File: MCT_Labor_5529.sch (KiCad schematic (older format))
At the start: 4 parts

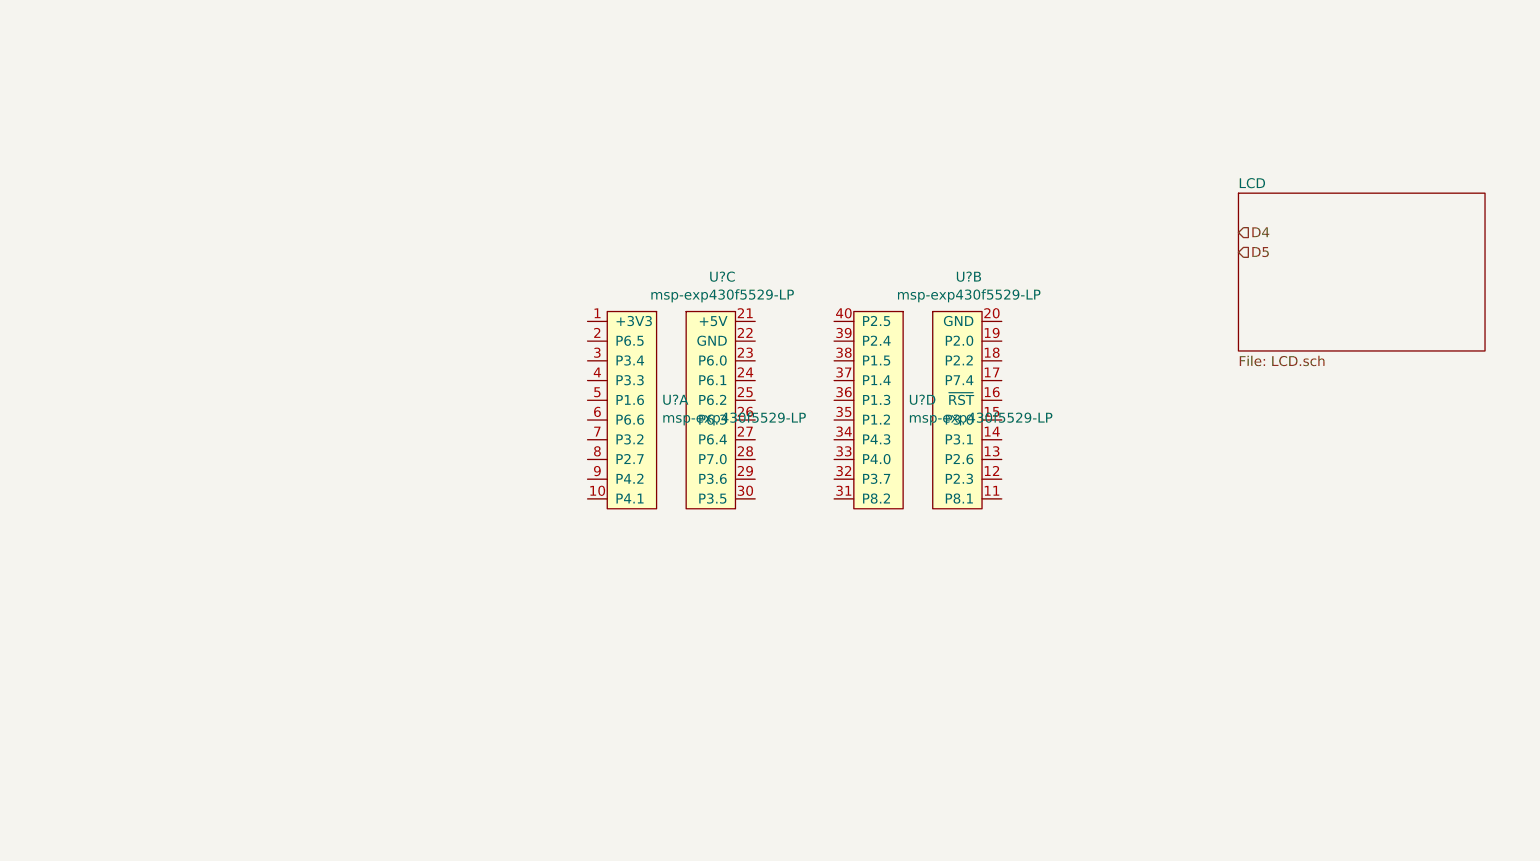
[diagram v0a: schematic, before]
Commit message: Schaltplan angefangen
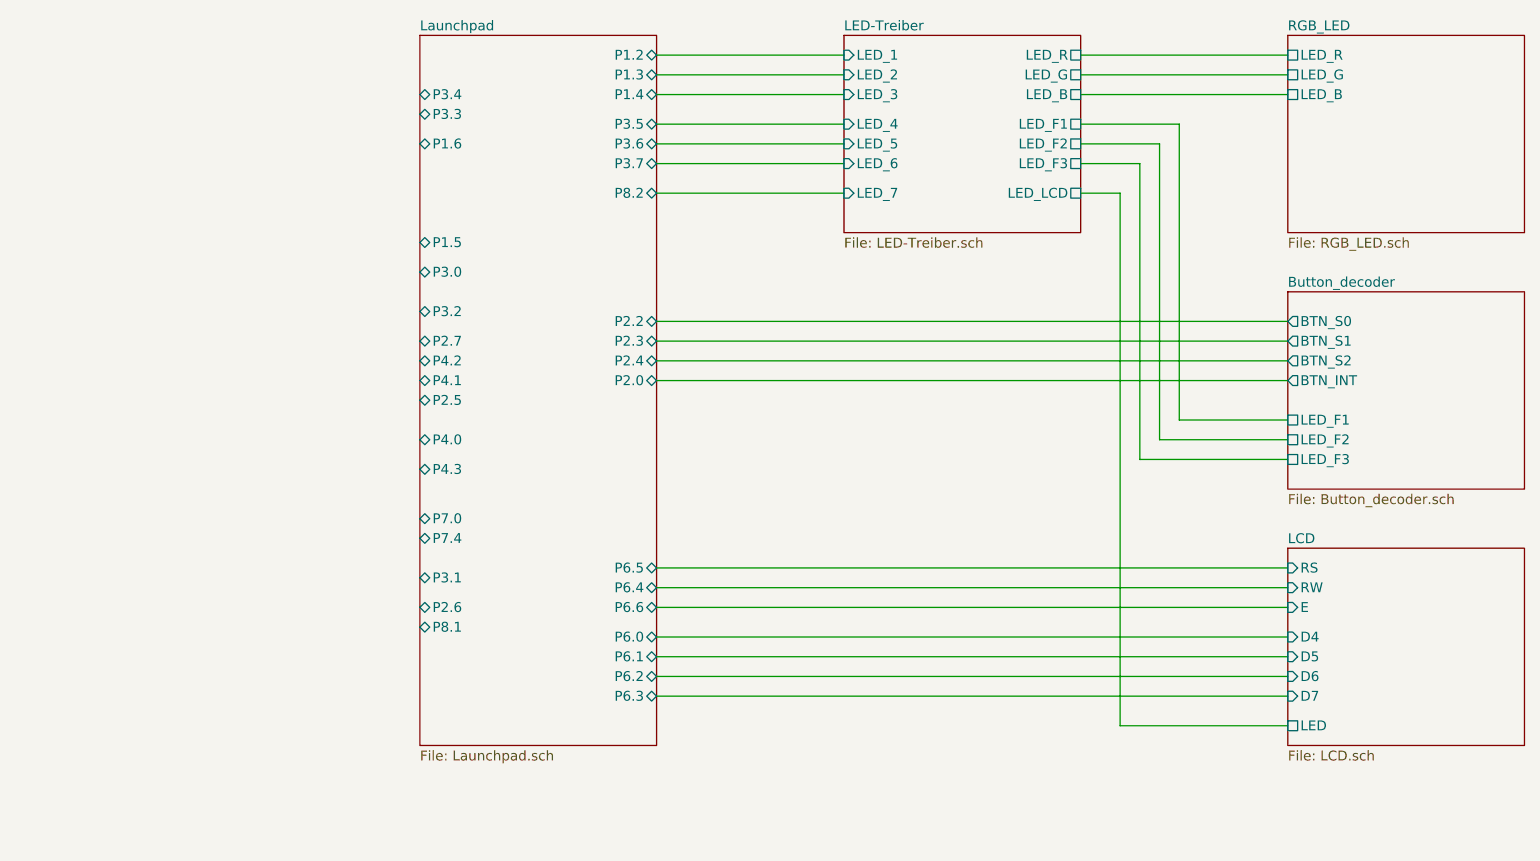
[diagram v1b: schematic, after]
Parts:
- removed U? (x4): msp-exp430f5529-LP, symbol HS-Wismar:msp-exp430f5529-LP
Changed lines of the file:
@@
 $Descr A4 11693 8268
 encoding utf-8
-Sheet 1 2
+Sheet 1 6
 Title ""
 Date ""
@@
 Comment4 ""
 $EndDescr
-$Comp
-L HS-Wismar:msp-exp430f5529-LP U?
-U 1 1 5EE8B2E3
-P 5550 3950
-F 0 "U?" H 5522 4501 50  0000 R CNN
-F 1 "msp-exp430f5529-LP" H 5522 4410 50  0000 R CNN
-F 2 "" H 5550 3950 50  0001 C CNN
-F 3 "" H 5550 3950 50  0001 C CNN
-	1    5550 3950
-	-1   0    0    -1
-$EndComp
-$Comp
-L HS-Wismar:msp-exp430f5529-LP U?
-U 2 1 5EE8BD9B
-P 6950 3950
-F 0 "U?" H 7133 5125 50  0000 C CNN
-F 1 "msp-exp430f5529-LP" H 7133 5034 50  0000 C CNN
-F 2 "" H 6950 3950 50  0001 C CNN
-F 3 "" H 6950 3950 50  0001 C CNN
-	2    6950 3950
-	1    0    0    -1
-$EndComp
-$Comp
-L HS-Wismar:msp-exp430f5529-LP U?
-U 3 1 5EE8C0BE
-P 5700 3950
-F 0 "U?" H 5883 5125 50  0000 C CNN
-F 1 "msp-exp430f5529-LP" H 5883 5034 50  0000 C CNN
-F 2 "" H 5700 3950 50  0001 C CNN
-F 3 "" H 5700 3950 50  0001 C CNN
-	3    5700 3950
-	1    0    0    -1
-$EndComp
-$Comp
-L HS-Wismar:msp-exp430f5529-LP U?
-U 4 1 5EE8CABB
-P 6800 3950
-F 0 "U?" H 6772 4501 50  0000 R CNN
-F 1 "msp-exp430f5529-LP" H 6772 4410 50  0000 R CNN
-F 2 "" H 6800 3950 50  0001 C CNN
-F 3 "" H 6800 3950 50  0001 C CNN
-	4    6800 3950
-	-1   0    0    -1
-$EndComp
 $Sheet
-S 8500 2350 1250 800
+S 8750 4150 1200 1000
 U 5EE928F9
 F0 "LCD" 50
 F1 "LCD.sch" 50
+F2 "D4" I L 8750 4600 50
+F3 "D5" I L 8750 4700 50
+F4 "D6" I L 8750 4800 50
+F5 "D7" I L 8750 4900 50
+F6 "RS" I L 8750 4250 50
+F7 "RW" I L 8750 4350 50
+F8 "E" I L 8750 4450 50
+F9 "LED" U L 8750 5050 50
 $EndSheet
-Text HLabel 8500 2550 2    50   Input ~ 0
-D4
-Text HLabel 8500 2650 2    50   Input ~ 0
-D5
+Wire Wire Line
+	8750 4900 5550 4900
+$Sheet
+S 6500 1550 1200 1000
+U 5EF68F99
+F0 "LED-Treiber" 50
+F1 "LED-Treiber.sch" 50
+F2 "LED_1" I L 6500 1650 50
+F3 "LED_2" I L 6500 1750 50
+F4 "LED_3" I L 6500 1850 50
+F5 "LED_4" I L 6500 2000 50
+F6 "LED_5" I L 6500 2100 50
+F7 "LED_6" I L 6500 2200 50
+F8 "LED_7" I L 6500 2350 50
+F9 "LED_R" U R 7700 1650 50
+F10 "LED_G" U R 7700 1750 50
+F11 "LED_B" U R 7700 1850 50
+F12 "LED_F1" U R 7700 2000 50
+F13 "LED_F2" U R 7700 2100 50
+F14 "LED_F3" U R 7700 2200 50
+F15 "LED_LCD" U R 7700 2350 50
+$EndSheet
+Wire Wire Line
+	7700 2350 7900 2350
+Wire Wire Line
+	7900 2350 7900 5050
+Wire Wire Line
+	7900 5050 8750 5050
+Wire Wire Line
+	6500 1650 5550 1650
+Wire Wire Line
+	5550 1750 6500 1750
+Wire Wire Line
+	6500 1850 5550 1850
+Wire Wire Line
+	5550 2000 6500 2000
+Wire Wire Line
+	5550 2100 6500 2100
+Wire Wire Line
+	5550 2200 6500 2200
+Wire Wire Line
+	5550 2350 6500 2350
+$Sheet
+S 8750 2850 1200 1000
+U 5EFA716B
+F0 "Button_decoder" 50
+F1 "Button_decoder.sch" 50
+F2 "BTN_S0" O L 8750 3000 50
+F3 "BTN_S1" O L 8750 3100 50
+F4 "BTN_S2" O L 8750 3200 50
+F5 "BTN_INT" O L 8750 3300 50
+F6 "LED_F1" U L 8750 3500 50
+F7 "LED_F2" U L 8750 3600 50
+F8 "LED_F3" U L 8750 3700 50
+$EndSheet
+Wire Wire Line
+	8200 2000 8200 3500
+Wire Wire Line
+	8200 3500 8750 3500
+Wire Wire Line
+	7700 2000 8200 2000
+Wire Wire Line
+	8750 3600 8100 3600
+Wire Wire Line
+	8100 3600 8100 2100
+Wire Wire Line
+	8100 2100 7700 2100
+Wire Wire Line
+	7700 2200 8000 2200
+Wire Wire Line
+	8000 2200 8000 3700
+Wire Wire Line
+	8000 3700 8750 3700
+$Sheet
+S 8750 1550 1200 1000
+U 5F03A5E7
+F0 "RGB_LED" 50
+F1 "RGB_LED.sch" 50
+F2 "LED_R" U L 8750 1650 50
+F3 "LED_G" U L 8750 1750 50
+F4 "LED_B" U L 8750 1850 50
+$EndSheet
+Wire Wire Line
+	7700 1650 8750 1650
+Wire Wire Line
+	8750 1750 7700 1750
+Wire Wire Line
+	7700 1850 8750 1850
+Wire Wire Line
+	5550 4800 8750 4800
+Wire Wire Line
+	5550 4700 8750 4700
+Wire Wire Line
+	5550 4600 8750 4600
+Wire Wire Line
+	5550 4450 8750 4450
+Wire Wire Line
+	5550 4350 8750 4350
+Wire Wire Line
+	5550 4250 8750 4250
+Wire Wire Line
+	5550 3300 8750 3300
+Wire Wire Line
+	5550 3200 8750 3200
+Wire Wire Line
+	5550 3100 8750 3100
+Wire Wire Line
+	5550 3000 8750 3000
+$Sheet
+S 4350 1550 1200 3600
+U 5F0B42CA
+F0 "Launchpad" 50
+F1 "Launchpad.sch" 50
+F2 "P6.5" B R 5550 4250 50
+F3 "P3.4" B L 4350 1850 50
+F4 "P3.3" B L 4350 1950 50
+F5 "P1.6" B L 4350 2100 50
+F6 "P6.6" B R 5550 4450 50
+F7 "P3.2" B L 4350 2950 50
+F8 "P2.7" B L 4350 3100 50
+F9 "P4.2" B L 4350 3200 50
+F10 "P4.1" B L 4350 3300 50
+F11 "P2.5" B L 4350 3400 50
+F12 "P2.4" B R 5550 3200 50
+F13 "P1.5" B L 4350 2600 50
+F14 "P1.4" B R 5550 1850 50
+F15 "P1.3" B R 5550 1750 50
+F16 "P1.2" B R 5550 1650 50
+F17 "P4.3" B L 4350 3750 50
+F18 "P4.0" B L 4350 3600 50
+F19 "P3.7" B R 5550 2200 50
+F20 "P8.2" B R 5550 2350 50
+F21 "P6.0" B R 5550 4600 50
+F22 "P6.1" B R 5550 4700 50
+F23 "P6.2" B R 5550 4800 50
+F24 "P6.3" B R 5550 4900 50
+F25 "P6.4" B R 5550 4350 50
+F26 "P7.0" B L 4350 4000 50
+F27 "P3.6" B R 5550 2100 50
+F28 "P3.5" B R 5550 2000 50
+F29 "P2.0" B R 5550 3300 50
+F30 "P2.2" B R 5550 3000 50
+F31 "P7.4" B L 4350 4100 50
+F32 "P3.0" B L 4350 2750 50
+F33 "P3.1" B L 4350 4300 50
+F34 "P2.6" B L 4350 4450 50
+F35 "P2.3" B R 5550 3100 50
+F36 "P8.1" B L 4350 4550 50
+$EndSheet
 $EndSCHEMATC

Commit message: Blockschaltbild komplett v1
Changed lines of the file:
@@
 $Descr A4 11693 8268
 encoding utf-8
-Sheet 1 6
+Sheet 1 10
 Title ""
 Date ""
@@
 F1 "Launchpad.sch" 50
 F2 "P6.5" B R 5550 4250 50
-F3 "P3.4" B L 4350 1850 50
-F4 "P3.3" B L 4350 1950 50
-F5 "P1.6" B L 4350 2100 50
+F3 "P3.4" B L 4350 3250 50
+F4 "P3.3" B L 4350 3150 50
+F5 "P1.6" B L 4350 4850 50
 F6 "P6.6" B R 5550 4450 50
-F7 "P3.2" B L 4350 2950 50
-F8 "P2.7" B L 4350 3100 50
-F9 "P4.2" B L 4350 3200 50
-F10 "P4.1" B L 4350 3300 50
-F11 "P2.5" B L 4350 3400 50
+F7 "P3.2" B L 4350 1850 50
+F8 "P2.7" B L 4350 2650 50
+F9 "P4.2" B L 4350 4050 50
+F10 "P4.1" B L 4350 3950 50
+F11 "P2.5" B L 4350 2450 50
 F12 "P2.4" B R 5550 3200 50
-F13 "P1.5" B L 4350 2600 50
+F13 "P1.5" B L 4350 4750 50
 F14 "P1.4" B R 5550 1850 50
 F15 "P1.3" B R 5550 1750 50
 F16 "P1.2" B R 5550 1650 50
-F17 "P4.3" B L 4350 3750 50
-F18 "P4.0" B L 4350 3600 50
+F17 "P4.3" B L 4350 2200 50
+F18 "P4.0" B L 4350 2100 50
 F19 "P3.7" B R 5550 2200 50
 F20 "P8.2" B R 5550 2350 50
@@
 F24 "P6.3" B R 5550 4900 50
 F25 "P6.4" B R 5550 4350 50
-F26 "P7.0" B L 4350 4000 50
+F26 "P7.0" B L 4350 5050 50
 F27 "P3.6" B R 5550 2100 50
 F28 "P3.5" B R 5550 2000 50
 F29 "P2.0" B R 5550 3300 50
 F30 "P2.2" B R 5550 3000 50
-F31 "P7.4" B L 4350 4100 50
-F32 "P3.0" B L 4350 2750 50
-F33 "P3.1" B L 4350 4300 50
-F34 "P2.6" B L 4350 4450 50
+F31 "P7.4" B L 4350 2000 50
+F32 "P3.0" B L 4350 1650 50
+F33 "P3.1" B L 4350 1750 50
+F34 "P2.6" B L 4350 2550 50
 F35 "P2.3" B R 5550 3100 50
-F36 "P8.1" B L 4350 4550 50
-$EndSheet
+F36 "P8.1" B L 4350 2350 50
+F37 "~RST" O L 4350 3400 50
+$EndSheet
+$Sheet
+S 2300 1550 1200 1200
+U 5EF44B02
+F0 "SPI" 50
+F1 "SPI.sch" 50
+F2 "A0" I R 3500 2450 50
+F3 "A1" I R 3500 2550 50
+F4 "A2" I R 3500 2650 50
+F5 "ADDR_EN" I R 3500 2350 50
+F6 "MISO" O R 3500 1750 50
+F7 "MOSI" I R 3500 1650 50
+F8 "SCK" I R 3500 1850 50
+F9 "µSD_detect" O R 3500 2000 50
+F10 "NRF_CE" I R 3500 2100 50
+F11 "NRF_INT" O R 3500 2200 50
+$EndSheet
+Wire Wire Line
+	3500 1650 4350 1650
+Wire Wire Line
+	4350 1750 3500 1750
+Wire Wire Line
+	3500 1850 4350 1850
+Wire Wire Line
+	4350 2350 3500 2350
+Wire Wire Line
+	3500 2450 4350 2450
+Wire Wire Line
+	4350 2550 3500 2550
+Wire Wire Line
+	3500 2650 4350 2650
+$Sheet
+S 2300 3050 1200 500
+U 5EFA875F
+F0 "UART" 50
+F1 "UART.sch" 50
+F2 "RX_in" I R 3500 3150 50
+F3 "TX_out" O R 3500 3250 50
+F4 "~RST" I R 3500 3400 50
+$EndSheet
+$Sheet
+S 2300 3850 1200 500
+U 5EFA8860
+F0 "I2C" 50
+F1 "I2C.sch" 50
+F2 "SDA" B R 3500 3950 50
+F3 "SCL" I R 3500 4050 50
+$EndSheet
+Wire Wire Line
+	4350 2200 3500 2200
+Wire Wire Line
+	3500 2100 4350 2100
+Wire Wire Line
+	4350 2000 3500 2000
+$Sheet
+S 2300 4650 1200 500
+U 5EFB1255
+F0 "analog/Fan" 50
+F1 "analog.sch" 50
+F2 "pulse_out" O R 3500 4750 50
+F3 "PWM_in" I R 3500 4850 50
+F4 "analog" U R 3500 5050 50
+$EndSheet
+Wire Wire Line
+	4350 3400 3500 3400
+Wire Wire Line
+	4350 3150 3500 3150
+Wire Wire Line
+	3500 3250 4350 3250
+Wire Wire Line
+	3500 3950 4350 3950
+Wire Wire Line
+	3500 4050 4350 4050
+Wire Wire Line
+	3500 5050 4350 5050
+Wire Wire Line
+	4350 4850 3500 4850
+Wire Wire Line
+	3500 4750 4350 4750
 $EndSCHEMATC

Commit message: Erste fertige Version
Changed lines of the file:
@@
 $EndDescr
 $Sheet
-S 8750 4150 1200 1000
+S 8750 4550 1200 1000
 U 5EE928F9
 F0 "LCD" 50
 F1 "LCD.sch" 50
-F2 "D4" I L 8750 4600 50
-F3 "D5" I L 8750 4700 50
-F4 "D6" I L 8750 4800 50
-F5 "D7" I L 8750 4900 50
-F6 "RS" I L 8750 4250 50
-F7 "RW" I L 8750 4350 50
-F8 "E" I L 8750 4450 50
-F9 "LED" U L 8750 5050 50
-$EndSheet
-Wire Wire Line
-	8750 4900 5550 4900
+F2 "D4" I L 8750 5000 50
+F3 "D5" I L 8750 5100 50
+F4 "D6" I L 8750 5200 50
+F5 "D7" I L 8750 5300 50
+F6 "RS" I L 8750 4750 50
+F7 "R~W~" I L 8750 4650 50
+F8 "E" I L 8750 4850 50
+F9 "LED" U L 8750 5450 50
+$EndSheet
+Wire Wire Line
+	8750 5300 5550 5300
 $Sheet
 S 6500 1550 1200 1000
@@
 	7700 2350 7900 2350
 Wire Wire Line
-	7900 2350 7900 5050
-Wire Wire Line
-	7900 5050 8750 5050
+	7900 2350 7900 5450
+Wire Wire Line
+	7900 5450 8750 5450
 Wire Wire Line
 	6500 1650 5550 1650
@@
 	5550 2350 6500 2350
 $Sheet
-S 8750 2850 1200 1000
+S 8750 3000 1200 1000
 U 5EFA716B
 F0 "Button_decoder" 50
 F1 "Button_decoder.sch" 50
-F2 "BTN_S0" O L 8750 3000 50
-F3 "BTN_S1" O L 8750 3100 50
-F4 "BTN_S2" O L 8750 3200 50
-F5 "BTN_INT" O L 8750 3300 50
-F6 "LED_F1" U L 8750 3500 50
-F7 "LED_F2" U L 8750 3600 50
-F8 "LED_F3" U L 8750 3700 50
-$EndSheet
-Wire Wire Line
-	8200 2000 8200 3500
-Wire Wire Line
-	8200 3500 8750 3500
+F2 "BTN_S0" O L 8750 3150 50
+F3 "BTN_S1" O L 8750 3250 50
+F4 "BTN_S2" O L 8750 3350 50
+F5 "BTN_INT" O L 8750 3450 50
+F6 "LED_F1" U L 8750 3650 50
+F7 "LED_F2" U L 8750 3750 50
+F8 "LED_F3" U L 8750 3850 50
+$EndSheet
 Wire Wire Line
 	7700 2000 8200 2000
 Wire Wire Line
-	8750 3600 8100 3600
-Wire Wire Line
-	8100 3600 8100 2100
-Wire Wire Line
 	8100 2100 7700 2100
 Wire Wire Line
 	7700 2200 8000 2200
-Wire Wire Line
-	8000 2200 8000 3700
-Wire Wire Line
-	8000 3700 8750 3700
 $Sheet
 S 8750 1550 1200 1000
@@
 	7700 1850 8750 1850
 Wire Wire Line
-	5550 4800 8750 4800
-Wire Wire Line
-	5550 4700 8750 4700
-Wire Wire Line
-	5550 4600 8750 4600
-Wire Wire Line
-	5550 4450 8750 4450
-Wire Wire Line
-	5550 4350 8750 4350
-Wire Wire Line
-	5550 4250 8750 4250
-Wire Wire Line
-	5550 3300 8750 3300
-Wire Wire Line
-	5550 3200 8750 3200
-Wire Wire Line
-	5550 3100 8750 3100
-Wire Wire Line
-	5550 3000 8750 3000
-$Sheet
-S 4350 1550 1200 3600
-U 5F0B42CA
-F0 "Launchpad" 50
-F1 "Launchpad.sch" 50
-F2 "P6.5" B R 5550 4250 50
-F3 "P3.4" B L 4350 3250 50
-F4 "P3.3" B L 4350 3150 50
-F5 "P1.6" B L 4350 4850 50
-F6 "P6.6" B R 5550 4450 50
-F7 "P3.2" B L 4350 1850 50
-F8 "P2.7" B L 4350 2650 50
-F9 "P4.2" B L 4350 4050 50
-F10 "P4.1" B L 4350 3950 50
-F11 "P2.5" B L 4350 2450 50
-F12 "P2.4" B R 5550 3200 50
-F13 "P1.5" B L 4350 4750 50
-F14 "P1.4" B R 5550 1850 50
-F15 "P1.3" B R 5550 1750 50
-F16 "P1.2" B R 5550 1650 50
-F17 "P4.3" B L 4350 2200 50
-F18 "P4.0" B L 4350 2100 50
-F19 "P3.7" B R 5550 2200 50
-F20 "P8.2" B R 5550 2350 50
-F21 "P6.0" B R 5550 4600 50
-F22 "P6.1" B R 5550 4700 50
-F23 "P6.2" B R 5550 4800 50
-F24 "P6.3" B R 5550 4900 50
-F25 "P6.4" B R 5550 4350 50
-F26 "P7.0" B L 4350 5050 50
-F27 "P3.6" B R 5550 2100 50
-F28 "P3.5" B R 5550 2000 50
-F29 "P2.0" B R 5550 3300 50
-F30 "P2.2" B R 5550 3000 50
-F31 "P7.4" B L 4350 2000 50
-F32 "P3.0" B L 4350 1650 50
-F33 "P3.1" B L 4350 1750 50
-F34 "P2.6" B L 4350 2550 50
-F35 "P2.3" B R 5550 3100 50
-F36 "P8.1" B L 4350 2350 50
-F37 "~RST" O L 4350 3400 50
-$EndSheet
+	5550 5200 8750 5200
+Wire Wire Line
+	5550 5100 8750 5100
+Wire Wire Line
+	5550 5000 8750 5000
+Wire Wire Line
+	5550 4850 8750 4850
+Wire Wire Line
+	5550 4750 8750 4750
+Wire Wire Line
+	5550 4650 8750 4650
+Wire Wire Line
+	5550 3250 8750 3250
+Wire Wire Line
+	5550 3150 8750 3150
+Wire Wire Line
+	5550 3350 8750 3350
+Wire Wire Line
+	5550 3450 8750 3450
 $Sheet
 S 2300 1550 1200 1200
@@
 	3500 2650 4350 2650
 $Sheet
-S 2300 3050 1200 500
+S 2300 3050 1200 900
 U 5EFA875F
 F0 "UART" 50
@@
 F3 "TX_out" O R 3500 3250 50
 F4 "~RST" I R 3500 3400 50
-$EndSheet
-$Sheet
-S 2300 3850 1200 500
+F5 "XBEE_Sleep_RQ" I R 3500 3550 50
+F6 "XBEE_~CTS~" O R 3500 3650 50
+F7 "XBEE_~RTS~" I R 3500 3750 50
+F8 "XBEE_RSSI" O R 3500 3850 50
+$EndSheet
+$Sheet
+S 2300 4250 1200 500
 U 5EFA8860
 F0 "I2C" 50
 F1 "I2C.sch" 50
-F2 "SDA" B R 3500 3950 50
-F3 "SCL" I R 3500 4050 50
+F2 "SDA" B R 3500 4350 50
+F3 "SCL" I R 3500 4450 50
 $EndSheet
 Wire Wire Line
@@
 	4350 2000 3500 2000
 $Sheet
-S 2300 4650 1200 500
+S 2300 5050 1200 500
 U 5EFB1255
 F0 "analog/Fan" 50
 F1 "analog.sch" 50
-F2 "pulse_out" O R 3500 4750 50
-F3 "PWM_in" I R 3500 4850 50
-F4 "analog" U R 3500 5050 50
+F2 "pulse_out" O R 3500 5250 50
+F3 "PWM_in" I R 3500 5150 50
+F4 "analog" U R 3500 5450 50
 $EndSheet
 Wire Wire Line
@@
 	3500 3250 4350 3250
 Wire Wire Line
-	3500 3950 4350 3950
-Wire Wire Line
-	3500 4050 4350 4050
-Wire Wire Line
-	3500 5050 4350 5050
-Wire Wire Line
-	4350 4850 3500 4850
-Wire Wire Line
-	3500 4750 4350 4750
+	3500 4450 4350 4450
+$Sheet
+S 4350 1550 1200 4000
+U 5F0B42CA
+F0 "Launchpad" 50
+F1 "Launchpad.sch" 50
+F2 "P6.5" B R 5550 4750 50
+F3 "P3.4" B L 4350 3250 50
+F4 "P3.3" B L 4350 3150 50
+F5 "P1.6" B L 4350 5250 50
+F6 "P6.6" B R 5550 4850 50
+F7 "P3.2" B L 4350 1850 50
+F8 "P2.7" B L 4350 2650 50
+F9 "P4.2" B L 4350 4450 50
+F10 "P4.1" B L 4350 4350 50
+F11 "P2.5" B L 4350 2450 50
+F12 "P2.4" B R 5550 3350 50
+F13 "P4.3" B L 4350 2200 50
+F14 "P4.0" B L 4350 2100 50
+F15 "P3.7" B R 5550 2200 50
+F16 "P8.2" B R 5550 2350 50
+F17 "P6.0" B R 5550 5000 50
+F18 "P6.1" B R 5550 5100 50
+F19 "P6.2" B R 5550 5200 50
+F20 "P6.3" B R 5550 5300 50
+F21 "P6.4" B R 5550 4650 50
+F22 "P7.0" B L 4350 5450 50
+F23 "P3.6" B R 5550 2100 50
+F24 "P3.5" B R 5550 2000 50
+F25 "P2.0" B R 5550 3450 50
+F26 "P2.2" B R 5550 3150 50
+F27 "P7.4" B L 4350 2000 50
+F28 "P3.0" B L 4350 1650 50
+F29 "P3.1" B L 4350 1750 50
+F30 "P2.6" B L 4350 2550 50
+F31 "P2.3" B R 5550 3250 50
+F32 "P8.1" B L 4350 2350 50
+F33 "~RST" O L 4350 3400 50
+F34 "P1.4_LED" B R 5550 1850 50
+F35 "P1.3_LED" B R 5550 1750 50
+F36 "P1.2_LED" B R 5550 1650 50
+F37 "P1.2_XBEE" B L 4350 3550 50
+F38 "P1.3_XBEE" B L 4350 3650 50
+F39 "P1.4_XBEE" B L 4350 3750 50
+F40 "P1.5_FAN" B L 4350 5150 50
+F41 "P1.5_XBEE" B L 4350 3850 50
+$EndSheet
+Wire Wire Line
+	3500 3550 4350 3550
+Wire Wire Line
+	4350 3650 3500 3650
+Wire Wire Line
+	3500 3750 4350 3750
+Wire Wire Line
+	3500 5450 4350 5450
+Wire Wire Line
+	4350 5150 3500 5150
+Wire Wire Line
+	3500 4350 4350 4350
+Wire Wire Line
+	3500 5250 4350 5250
+Wire Wire Line
+	3500 3850 4350 3850
+Wire Wire Line
+	8000 3850 8750 3850
+Wire Wire Line
+	8000 2200 8000 3850
+Wire Wire Line
+	8750 3750 8100 3750
+Wire Wire Line
+	8100 2100 8100 3750
+Wire Wire Line
+	8200 3650 8750 3650
+Wire Wire Line
+	8200 2000 8200 3650
 $EndSCHEMATC
